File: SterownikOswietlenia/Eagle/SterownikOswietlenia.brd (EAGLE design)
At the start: 100 x 80 mm, 15 parts, among them IC1 MEGA8-AI, T1 BT138-V

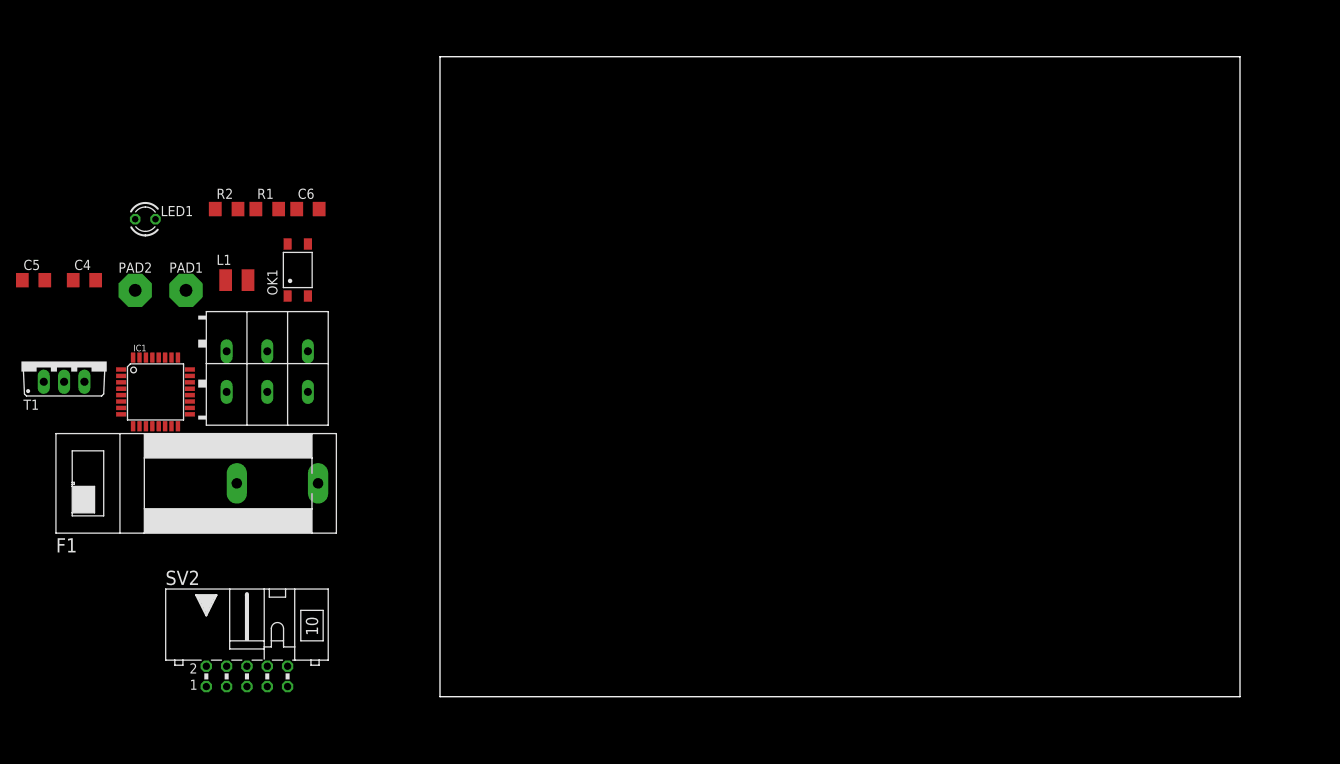
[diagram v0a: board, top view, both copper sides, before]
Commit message: uporzą▲dkowane opisy elementów
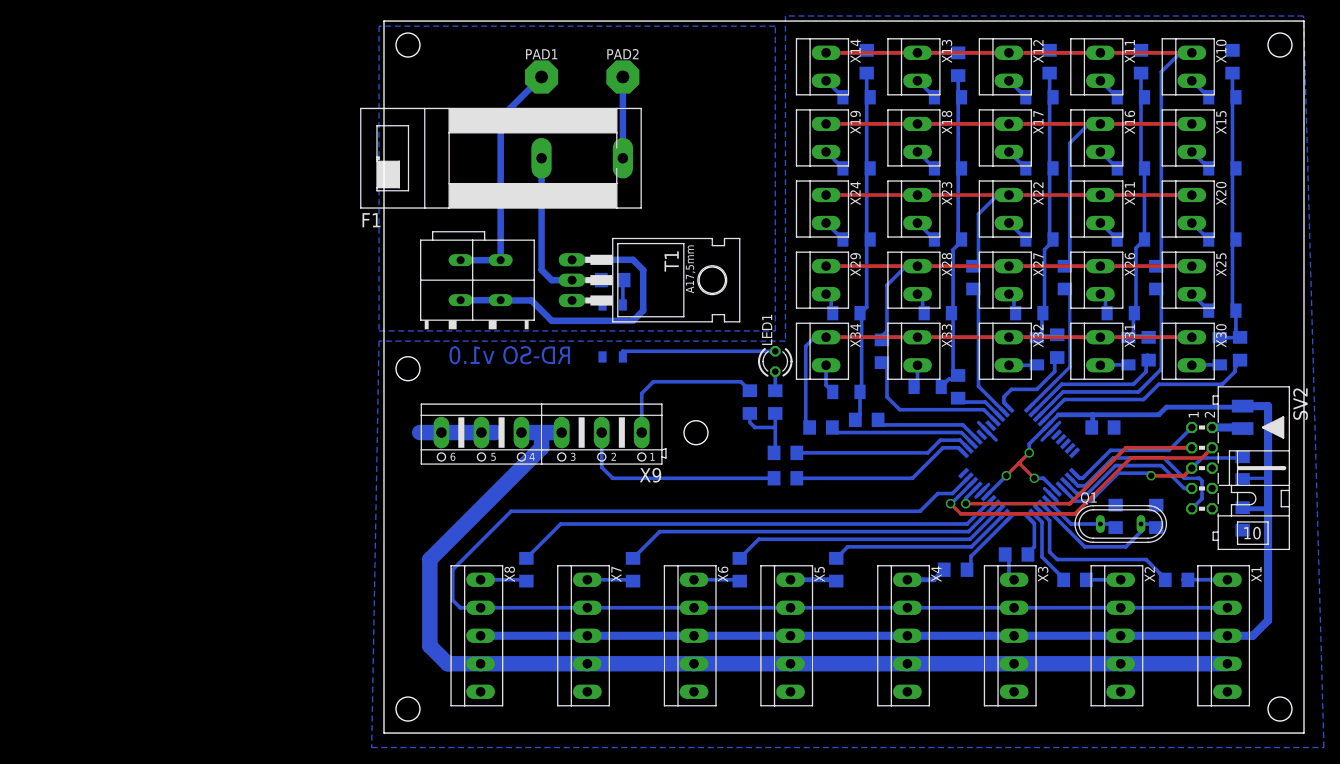
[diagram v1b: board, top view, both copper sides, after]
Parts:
- removed C6: 100n, rcl:C1206
- removed U$2: AK3001-3, RD:AK3001-3
- added C1, C2: 22p, rcl:C1206
- added D1, D10, D11, D12, D13, D14, D15, D16, D17, D18, D19, D2, D20, D21, D22, D23, D24, D25, D3, D4, D5, D6, D7, D8, D9: 1N4148, diode:MINIMELF
- added Q1: 12MHz, special:QS
- added R10, R11, R12, R13, R14, R15, R16, R17, R18, R19, R20, R21, R22, R23, R24, R25, R26, R27, R29, R8, R9: 100, rcl:R1206
- added R28: 10k, rcl:R1206
- added R3, R4, R5, R6, R7: 1k, rcl:R1206
- added U$1: AK3001-2, RD:AK3001-2
- added X1, X2, X3, X4, X5, X6, X7, X8: (no value), con-ria-59:5POL35
- added X10, X11, X12, X13, X14, X15, X16, X17, X18, X19, X20, X21, X22, X23, X24, X25, X26, X27, X28, X29, X30, X31, X32, X33, X34: (no value), con-ria-59:2POL35
- added X9: (no value), con-ptr500:AK500/6
- IC1: value MEGA8-AI -> MEGA32-A; device atmel:TQFP32-08 -> atmel:TQFP44
- T1: value BT138-V -> BT138-H; device triac:TO220BV -> triac:TO220BH
- moved C5 154.0 mm to (100.3, 22.2), flipped to the bottom, turned to 270 degrees
- moved C4 128.6 mm to (82.9, 33.7), flipped to the bottom, turned to 180 degrees
- moved L1 126.9 mm to (100.3, 34.9), flipped to the bottom, turned to 270 degrees
- moved SV2 122.2 mm to (95.2, 28.6), turned to 270 degrees
- moved IC1 108.3 mm to (72.4, 29.2), flipped to the bottom, turned to 45 degrees
- moved LED1 80.7 mm to (41.9, 41.9), turned to 90 degrees
- moved T1 70.6 mm to (22.9, 52.1), turned to 270 degrees
- moved R1 67.9 mm to (41.9, 36.8), flipped to the bottom, turned to 90 degrees
- moved PAD2 66.5 mm to (22.9, 77.5)
- moved F1 55.7 mm to (17.8, 67.3)
- moved PAD1 51.8 mm to (12.7, 77.5)
- moved R2 49.1 mm to (21.6, 52.1), flipped to the bottom
- moved OK1 40.1 mm to (21.6, 45.7), flipped to the bottom
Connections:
- new net +24V: X1.4, X2.4, X3.4, X4.4, X5.4, X6.4, X7.4, X8.4, X9.3, X9.4
- new net BTN-H-0: IC1.36, R8.1
- new net BTN-H-1: IC1.34, R9.1
- new net BTN-H-2: IC1.32, R10.1
- new net BTN-H-3: IC1.30, R11.1
- new net BTN-H-4: IC1.25, R12.1
- new net BTN-V-0: IC1.37, R25.2
- new net BTN-V-1: IC1.35, R24.2
- new net BTN-V-2: IC1.33, R23.2
- new net BTN-V-3: IC1.31, R22.2
- new net BTN-V-4: IC1.26, R21.2
- new net LED-CKO-0: IC1.9, R13.2
- new net LED-CKO-1: IC1.10, R14.2
- new net LED-CKO-2: IC1.11, R15.2
- new net LED-CKO-3: IC1.12, R16.2
- new net LED-CKO-4: IC1.13, R17.2
- new net LED-CKO-5: IC1.14, R18.2
- new net LED-CKO-6: IC1.15, R19.2
- new net LED-CKO-7: IC1.16, R20.2
- new net LED-SDO: IC1.21, X1.2, X2.2, X3.2, X4.2, X5.2, X6.2, X7.2, X8.2
- new net M$44: R12.2, X30.1, X31.1, X32.1, X33.1, X34.1
- new net N$10: D2.A, X11.2
- new net N$113: D10.C, D15.C, D20.C, D25.C, D5.C, R21.1, R7.2
- new net N$12: D3.A, X12.2
- new net N$13: D4.A, X13.2
- new net N$131: D14.C, D19.C, D24.C, D4.C, D9.C, R22.1, R6.2
- new net N$132: D13.C, D18.C, D23.C, D3.C, D8.C, R23.1, R5.2
- new net N$133: D12.C, D17.C, D2.C, D22.C, D7.C, R24.1, R4.2
- new net N$134: D1.C, D11.C, D16.C, D21.C, D6.C, R25.1, R3.2
- new net N$14: R14.1, X2.1
- new net N$15: R15.1, X3.1
- new net N$16: R16.1, X4.1
- new net N$17: R17.1, X5.1
- new net N$18: D5.A, X14.2
- new net N$19: D10.A, X19.2
- new net N$20: D9.A, X18.2
- new net N$21: D8.A, X17.2
- new net N$22: D7.A, X16.2
- new net N$23: D6.A, X15.2
- new net N$24: D11.A, X20.2
- new net N$25: D12.A, X21.2
- new net N$26: D13.A, X22.2
- new net N$27: D14.A, X23.2
- new net N$28: D15.A, X24.2
- new net N$29: D20.A, X29.2
- new net N$30: D19.A, X28.2
- new net N$32: D17.A, X26.2
- new net N$33: D16.A, X25.2
- new net N$34: D21.A, X30.2
- new net N$35: D22.A, X31.2
- new net N$36: D23.A, X32.2
- new net N$37: D24.A, X33.2
- new net N$38: D25.A, X34.2
- new net N$39: R18.1, X6.1
- new net N$40: R8.2, X10.1, X11.1, X12.1, X13.1, X14.1
- new net N$41: R9.2, X15.1, X16.1, X17.1, X18.1, X19.1
- new net N$42: R10.2, X20.1, X21.1, X22.1, X23.1, X24.1
- new net N$43: R11.2, X25.1, X26.1, X27.1, X28.1, X29.1
- new net N$44: R19.1, X7.1
- new net N$45: R20.1, X8.1
- new net N$46: C1.1, IC1.7, Q1.1
- new net N$47: C2.1, IC1.8, Q1.2
- new net N$49: R27.1, X9.2
- new net N$50: R26.1, X9.1
- new net N$51: IC1.24, R29.1
- new net N$52: D18.A, X27.2
- new net N$7: R13.1, X1.1
- new net N$9: D1.A, X10.2
- new net POWER-IO-0: IC1.23, R27.2
- new net TEST_FREQUENCY: IC1.42
- net AVCC: now also IC1.27; no longer IC1.18
- net GND: now also C1.2, C2.2, IC1.18, IC1.28, IC1.39, IC1.6, OK1.3, R3.1, R4.1, R5.1, R6.1, R7.1, X1.5, X2.5, X3.5, X4.5, X5.5, X6.5, X7.5, X8.5, X9.5, X9.6; no longer C6.2, IC1.21, IC1.3, IC1.5, LED1.K
- net I2C-SCL: now also IC1.19; no longer IC1.28
- net I2C-SDA: now also IC1.20; no longer IC1.27
- net ISP-MISO: now also IC1.2; no longer IC1.16
- net ISP-MOSI: now also IC1.1; no longer IC1.15
- net ISP-SCK: now also IC1.3; no longer IC1.17
- net LED-POWER: now also R26.2, R29.2; no longer IC1.30
- net N$1: now also U$1.P$3, U$1.P$4; no longer U$2.P$3, U$2.P$4
- net N$5: now also LED1.K, OK1.1; no longer LED1.A, OK1.3
- net N$6: now also LED1.A; no longer OK1.1
- net N$8: now also U$1.P$1, U$1.P$2; no longer U$2.P$1, U$2.P$2
- net RESET: now also IC1.4, R28.1; no longer IC1.29
- net VCC: now also IC1.17, IC1.38, IC1.5, R28.2, X1.3, X2.3, X3.3, X4.3, X5.3, X6.3, X7.3, X8.3; no longer C6.1, IC1.4, IC1.6
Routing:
- net VCC: track 0.00 -> 181.1 mm, vias 0 -> 3
- net LED-SDO: track 0.00 -> 170.2 mm
- net +24V: track 0.00 -> 138.1 mm
- net N$40: track 0.00 -> 75.2 mm
- net N$41: track 0.00 -> 66.2 mm
- net LED-CKO-7: track 0.00 -> 61.1 mm
- net M$44: track 0.00 -> 59.0 mm
- net N$43: track 0.00 -> 57.6 mm
- net N$42: track 0.00 -> 57.4 mm
- net LED-CKO-6: track 0.00 -> 48.1 mm
- net N$113: track 0.00 -> 45.2 mm
- net N$131: track 0.00 -> 42.2 mm
- net I2C-SDA: track 0.00 -> 40.7 mm, vias 0 -> 1
- net N$8: track 0.00 -> 38.9 mm
- net N$134: track 0.00 -> 37.4 mm
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- added copper zone on layer 16, net GND
- added copper zone on layer 16, net N$48
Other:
- board size 100 x 80 mm -> 115 x 89 mm
- board text added: "RD-SO v1.0"
